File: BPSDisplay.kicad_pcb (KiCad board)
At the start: 2 copper layers, 91.4 x 56 mm, 64 parts, among them J1 SWD, J2 CAN_Out, J3 CAN_Out, J5 CarPowerConnector, J6 CAN_LogicAnalyzer, J7 SPI0_LogicAnalyzer, J8 GEN_LogicAnalyzer, J9 USART_LogicAnalyzer, P1 Conn_02x20_Odd_Even, SW1 Reset, U1 STM32F413RHTx, U2 ADM3055E, U3 CDSOT23-T24CAN, U6 PDS1-S12-S5, U7 NCP1117-3.3_SOT223, Y1 8M

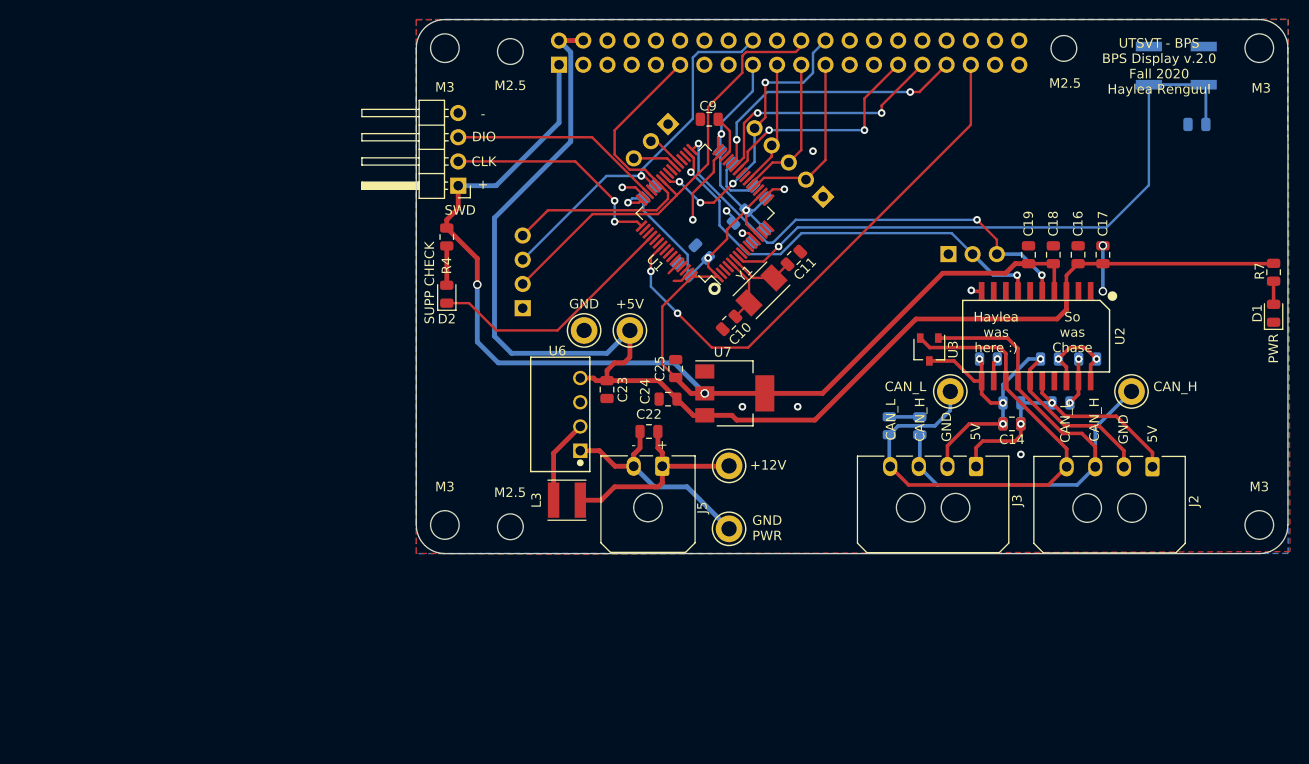
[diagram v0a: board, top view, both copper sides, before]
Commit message: Reorganized the board for practice using KiCAD
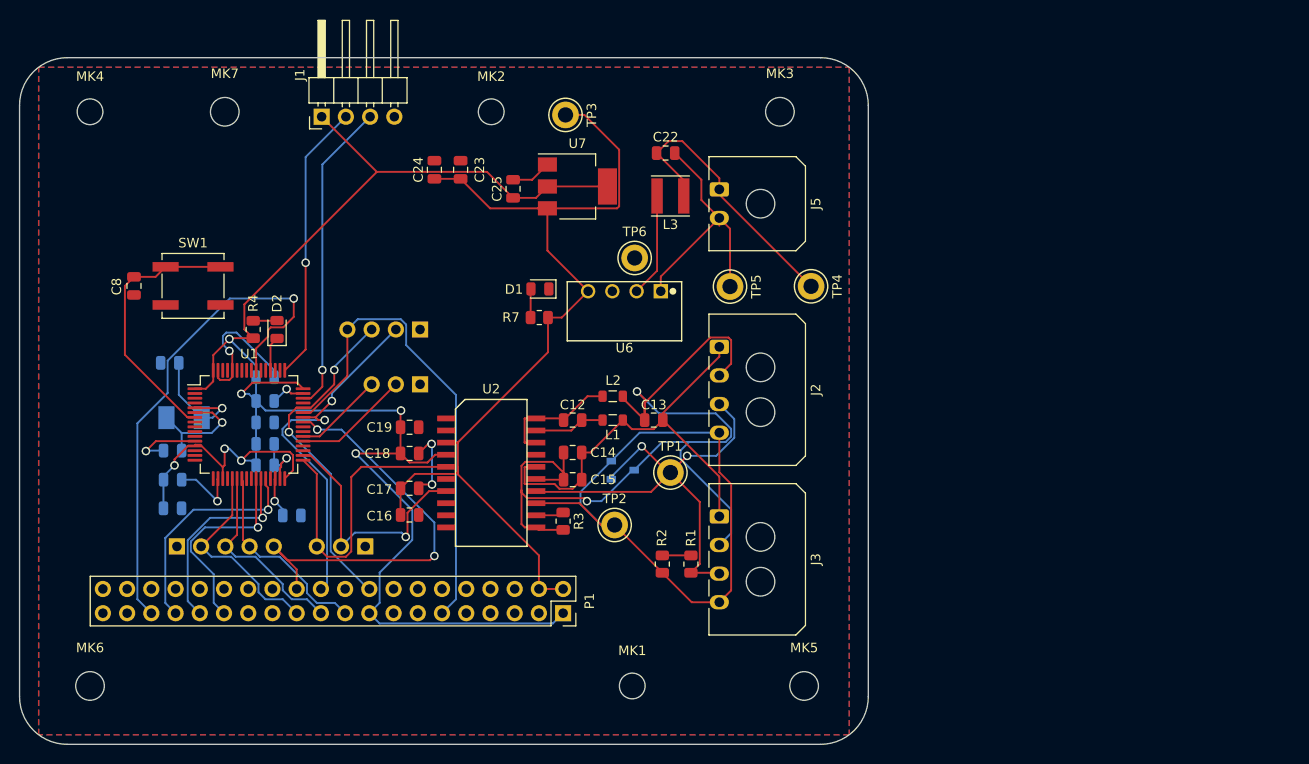
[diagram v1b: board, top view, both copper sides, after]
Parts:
- C10, C11, C9, U3, Y1: moved to B.Cu
- C12, C13, C15, C8, L1, L2, P1, R1, R2, R3, SW1: moved to F.Cu
- moved C8 112.7 mm to (160.0, 132.9), turned to 270 degrees
- moved SW1 105.7 mm to (166.2, 132.9)
- moved MK4 102.3 mm to (155.4, 114.7)
- moved LOGO1 84.6 mm to (190.2, 129.2), turned to 0 degrees
- moved R7 77.1 mm to (202.5, 136.2), turned to 180 degrees
- moved J7 77.0 mm to (164.5, 160.2), turned to 270 degrees
- moved D1 77.0 mm to (202.6, 133.2), turned to 180 degrees
- moved C17 76.7 mm to (188.9, 154.2), turned to 0 degrees
- moved MK6 76.5 mm to (155.4, 174.9)
- moved C16 75.2 mm to (188.9, 156.9), turned to 0 degrees
- moved C18 70.6 mm to (188.9, 150.5), turned to 0 degrees
- moved J6 68.4 mm to (184.2, 160.2), turned to 90 degrees
- moved C11 68.2 mm to (164.1, 150.2), turned to 180 degrees
- moved MK1 67.7 mm to (212.2, 174.9), turned to 0 degrees
- moved C19 67.4 mm to (188.9, 147.8), turned to 0 degrees
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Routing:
- net Net-(C13-Pad2): track 48.8 -> 98.7 mm, vias 4 -> 2
- net +5V: track 143.6 -> 100.7 mm
- net /NRST: track 67.1 -> 28.1 mm, vias 1 -> 0
- net Net-(D2-Pad1): track 26.8 -> 3.63 mm
- net GND: track 31.7 -> 52.4 mm, vias 12 -> 7
- net /CAN2_TX: track 46.1 -> 26.8 mm, vias 2 -> 1
- net /CAN2_RX: track 49.1 -> 32.1 mm, vias 3 -> 0
- net Net-(C13-Pad1): track 30.8 -> 45.8 mm, vias 2 -> 0
- net /GPIO8(SPI0_CE_N): track 30.4 -> 44.8 mm, vias 4 -> 2
- net /GPIO17(GEN0): track 37.0 -> 51.0 mm
- net /SWDIO: track 22.4 -> 32.9 mm, vias 0 -> 1
- net +3V3: track 183.6 -> 192.0 mm, vias 6 -> 7
- net /USART6_TX: track 3.85 -> 12.2 mm
- net /CAN/CAN_L: track 57.1 -> 65.2 mm
- net /GPIO25(GEN6): track 47.0 -> 38.9 mm, vias 0 -> 2
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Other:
- board size 91.4 x 56 mm -> 89 x 72 mm
- board text removed: "+"
- board text removed: "+12V"
- board text removed: "+5V"
- board text removed: "-"
- board text removed: "5V"
- board text removed: "BUSY"
- board text removed: "CAN"
- board text removed: "CAN_H"
- board text removed: "CAN_L"
- board text removed: "CLK"
- board text removed: "CS"
- board text removed: "DC"
- board text removed: "DIO"
- board text removed: "Dr. Gary Hallock"
- board text removed: "GEN"
- board text removed: "GND"
- board text removed: "GND PWR"
- board text removed: "Haylea was here :)"
- board text removed: "M2.5"
- board text removed: "M3"
- board text removed: "MISO"
- board text removed: "MOSI"
- board text removed: "PWR"
- board text removed: "RESET"
- board text removed: "RST"
- board text removed: "RX"
- board text removed: "SCK"
- board text removed: "SPIO"
- board text removed: "SUPP CHECK"
- board text removed: "SWD"
- board text removed: "So was Chase"
- board text removed: "TX"
- board text removed: "UART"
- board text removed: "UTSVT - BPS BPS Display v.2.0 Fall 2020 Haylea Renguul"

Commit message: reorganized PCB layout
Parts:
- moved MK1 0.75 mm to (213.0, 174.9)
